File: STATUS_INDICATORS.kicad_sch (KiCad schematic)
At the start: 0 parts

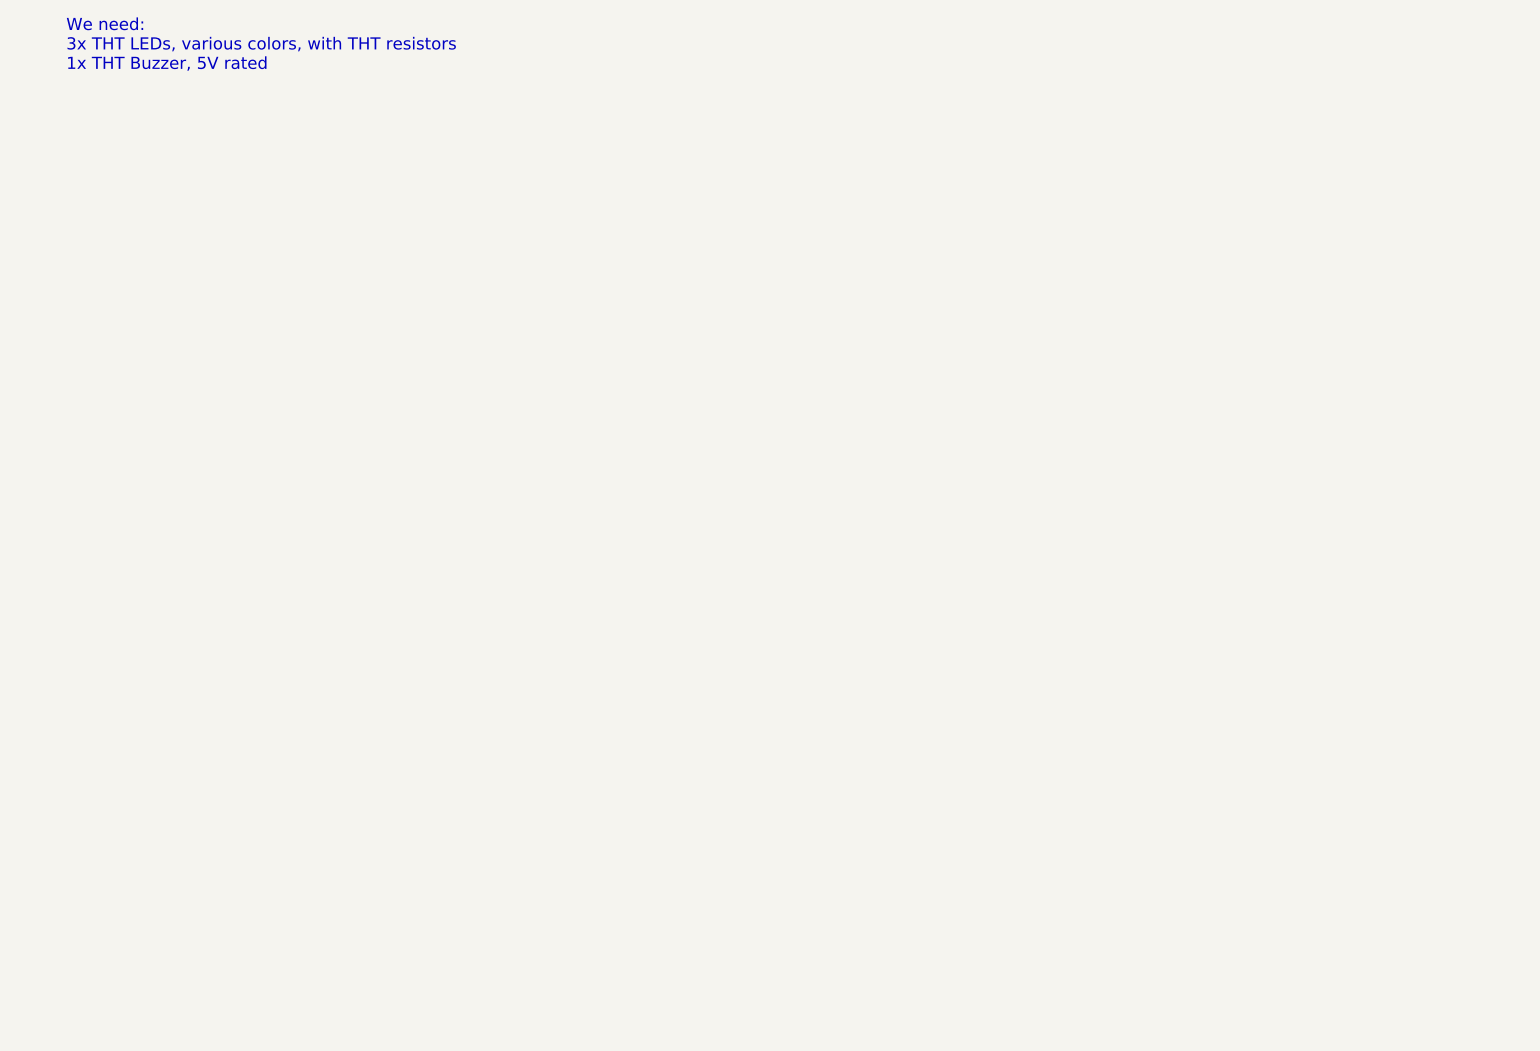
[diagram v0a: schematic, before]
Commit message: Merge relay and status schematic components
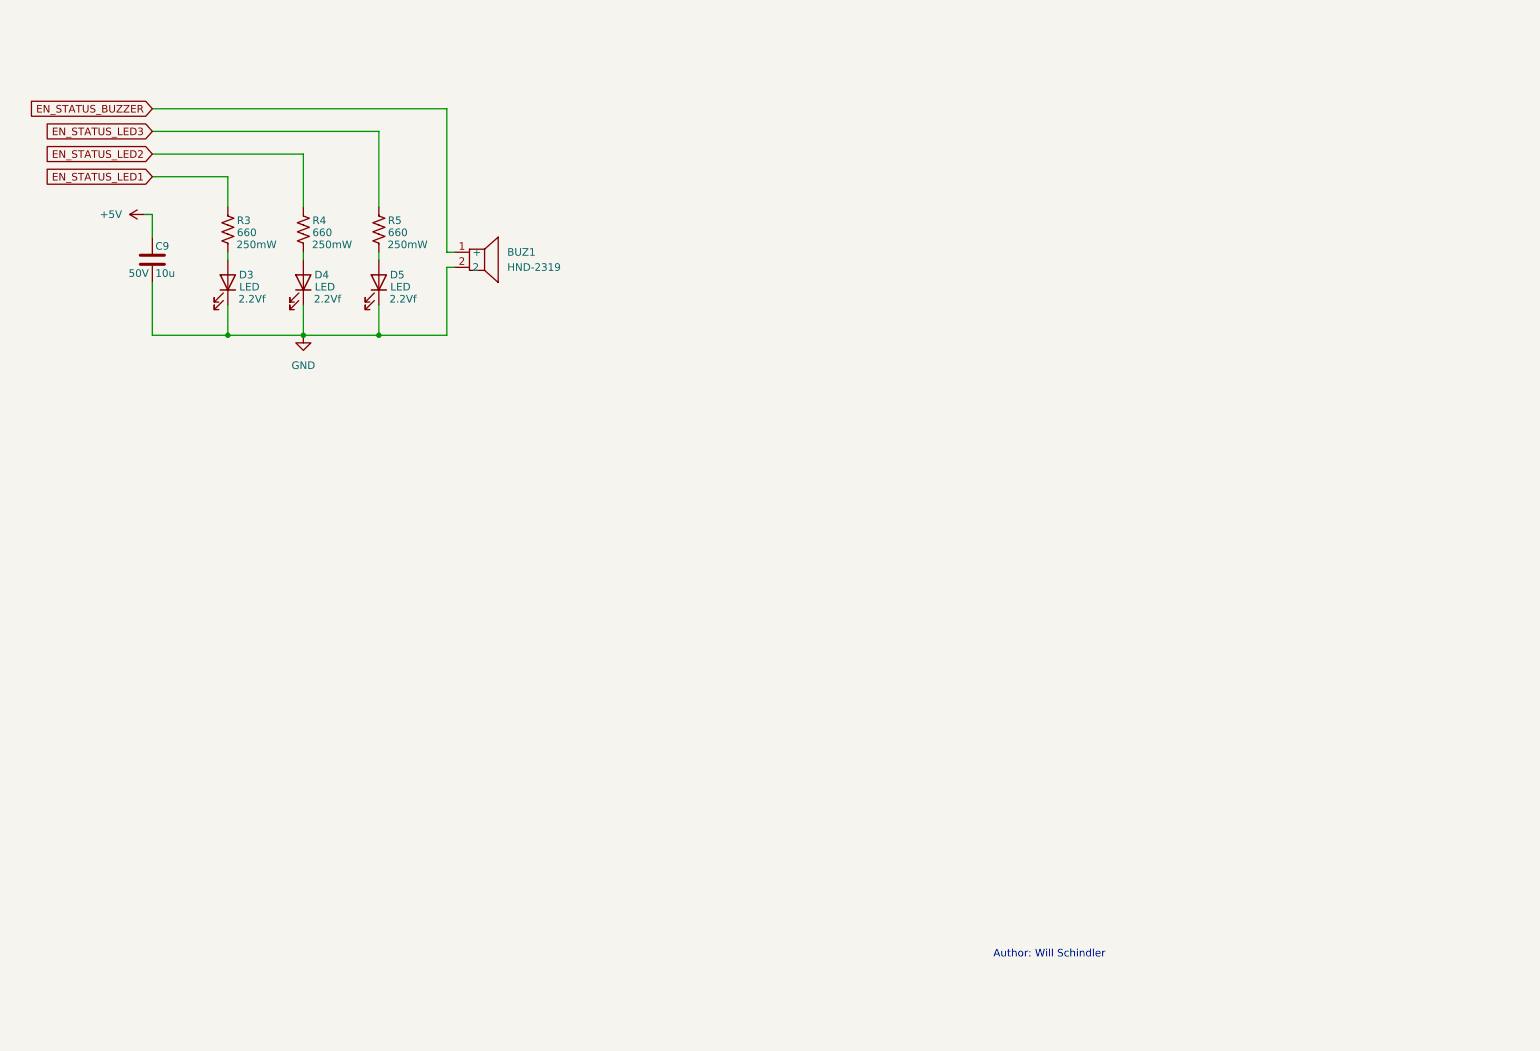
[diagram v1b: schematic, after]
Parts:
- added BUZ1: HND-2319, EasyEDA:BUZ-TH_BD23.0-P15.00-D0.8-FD, symbol EasyEDA:YD2319type
- added C9: 10u, EasyEDA:CAP-TH_L5.5-W3.8-P5.08-D0.5, symbol Device:C
- added D3, D4, D5: LED, EasyEDA:LED-TH_BD3.0-P2.54-FD_YELLOW, symbol Device:LED
- added R3, R4, R5: 660, EasyEDA:RES-TH_BD2.4-L6.3-P10.30-D0.6, symbol Device:R_US
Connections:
- new net: D5.2 (A), R5.2
- new net: D4.2 (A), R4.2
- new net: D3.2 (A), R3.2
- new net +5V: C9.1
- new net EN_STATUS_BUZZER: BUZ1.1 (+)
- new net EN_STATUS_LED1: R3.1
- new net EN_STATUS_LED2: R4.1
- new net EN_STATUS_LED3: R5.1
- new net GND: BUZ1.2, C9.2, D3.1 (K), D4.1 (K), D5.1 (K)
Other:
- note added: "Author: Will Schindler"
- note removed: "We need: 3x THT LEDs, various colors, with THT resistors 1x THT Buzzer, 5V rated"

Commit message: Cleanup schematics a little bit
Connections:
- net EN_STATUS_BUZZER renamed EN_STATUS_BUZZER1
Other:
- note added: "0"
- note added: "Authors: Isaac Subudhi Will Schindler"
- note added: "Mon, Oct, 12, 2026"
- note added: "RAM RACING: HUB V2: Status Indicators"
- note removed: "Author: Will Schindler"
- moved on the sheet: BUZ1, C9, D3, D4, D5, R3, R4, R5

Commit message: Mapping for M130, cleanup on all sheets, layout start
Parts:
- removed C9: 10u, EasyEDA:CAP-TH_L5.5-W3.8-P5.08-D0.5, symbol Device:C
- added C7: 100n, EasyEDA:CAP-TH_L5.0-W2.5-P5.00-D1.0, symbol Device:C
- BUZ1: now not fitted
- D1: renamed from D3; now not fitted
- D2: renamed from D4; now not fitted
- D3: renamed from D5; now not fitted
- R1: renamed from R3; now not fitted
- R2: renamed from R4; now not fitted
- R3: renamed from R5; now not fitted
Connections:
- net EN_STATUS_LED1 is gone; now on net +5V_B_AUX: R1.1
- net EN_STATUS_LED2 is gone; now on net +5V_B_AUX: R2.1
- net EN_STATUS_LED3 is gone; now on net +5V_B_AUX: R3.1
- net GND: now also C7.2; no longer BUZ1.2, D1.1 (K), D2.1 (K), D3.1 (K)
- net EN_STATUS_BUZZER1 renamed +5V_B_AUX
- net +5V_B_AUX: now also C7.1
- new net EN_LS_STATUS_BUZZER1: BUZ1.2
- new net EN_LS_STATUS_LED1: D1.1 (K)
- new net EN_LS_STATUS_LED2: D2.1 (K)
- new net EN_LS_STATUS_LED3: D3.1 (K)
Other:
- note added: "Authors: Lead: Isaac Subudhi Main Editor: Will Schindler"
- note removed: "Authors: Isaac Subudhi Will Schindler"
